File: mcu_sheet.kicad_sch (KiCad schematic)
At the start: 27 parts, among them IC1 STM32H523CET6, J1 Conn_01x05, SW1 SW_Push, SW2 SW_SPDT, Y1 Crystal_GND23, Y2 Crystal

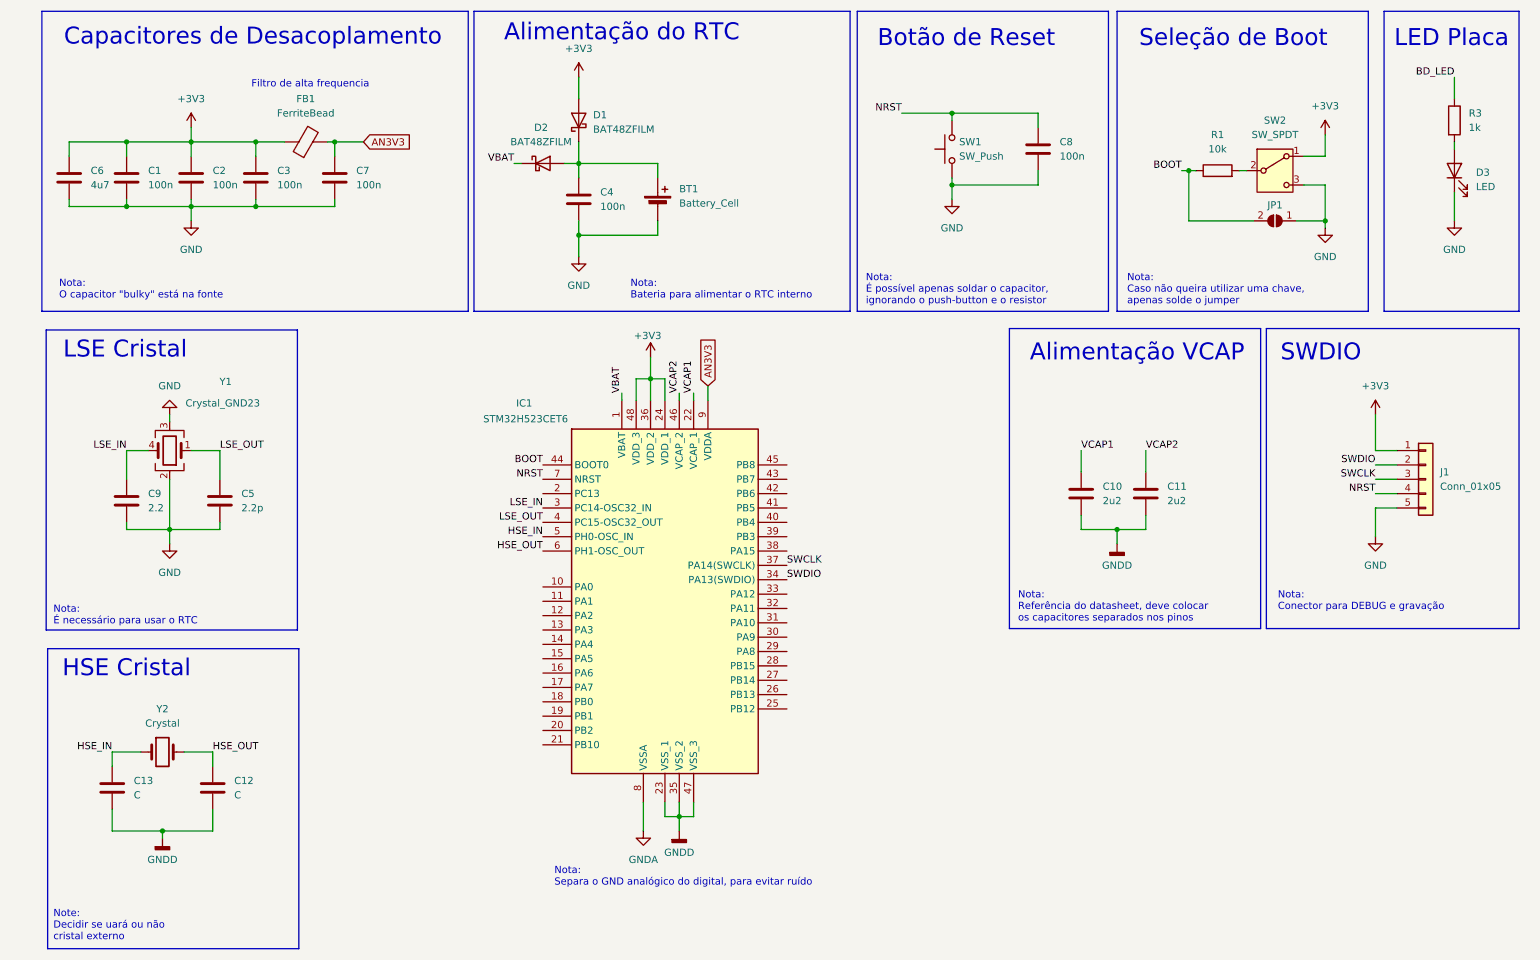
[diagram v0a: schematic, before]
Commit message: Alterei o nome para o par diferencial do CAN, adicionei capacitores de desacoplamento para todas as alimentacoes
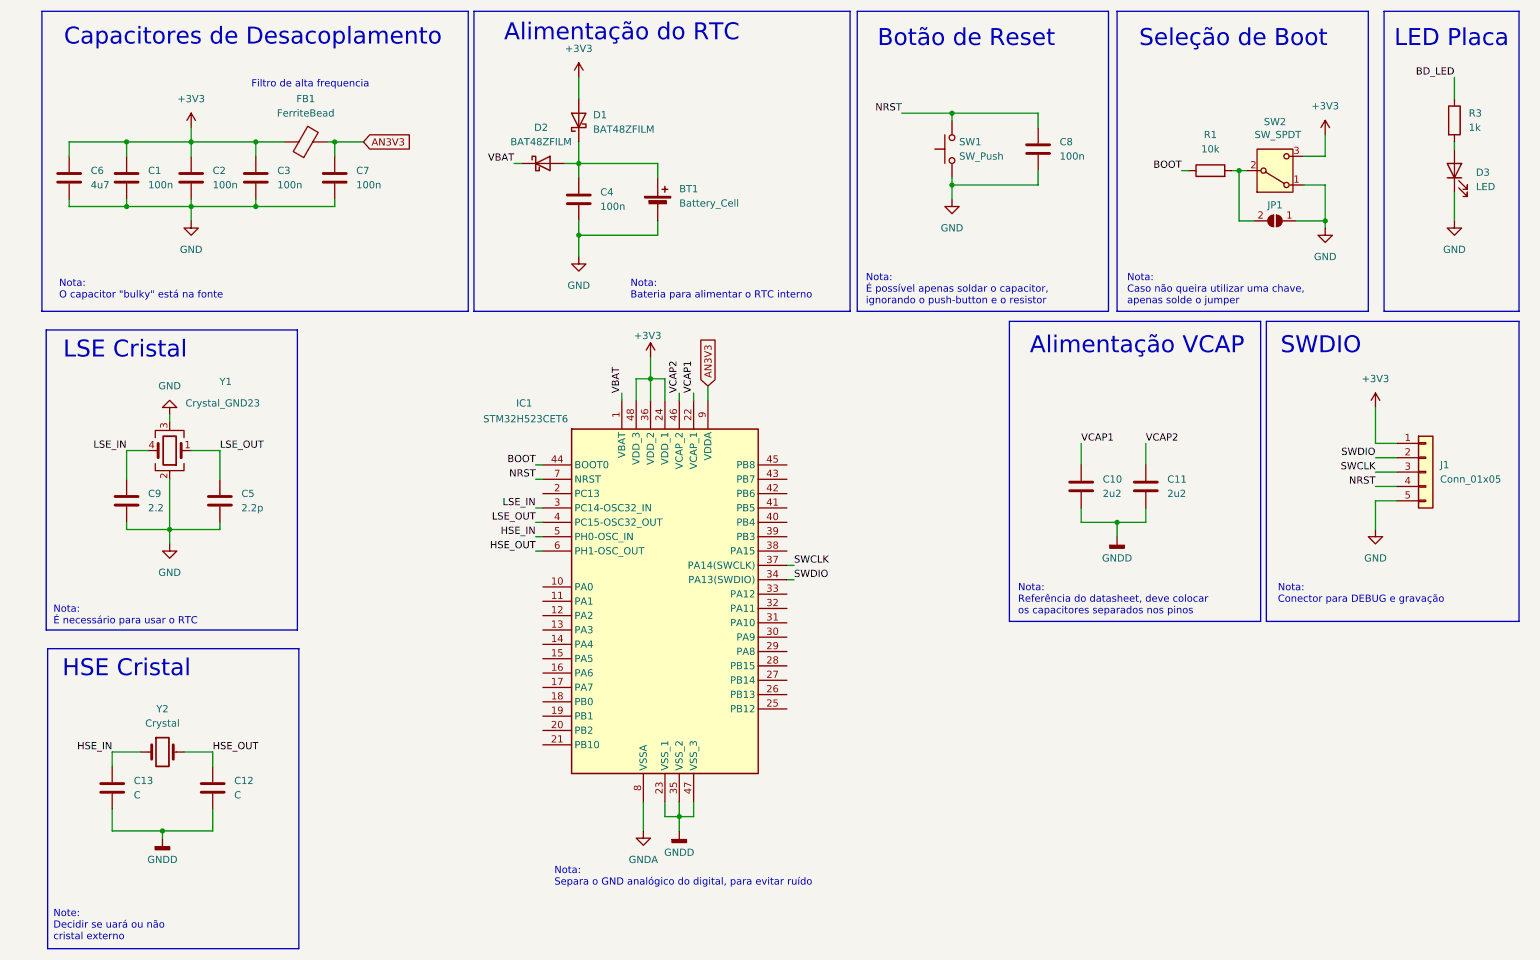
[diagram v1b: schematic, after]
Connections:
- net +3V3: now also SW2.3 (C); no longer SW2.1 (A)
- net BOOT: no longer JP1.2 (B)
- net GND: now also SW2.1 (A); no longer SW2.3 (C)
- net at R1.2, SW2.2 (B): now also JP1.2 (B)
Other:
- moved on the sheet: C10, C11, J1, R1

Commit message: Removi as entradas analógicas, projeto delas estava errado
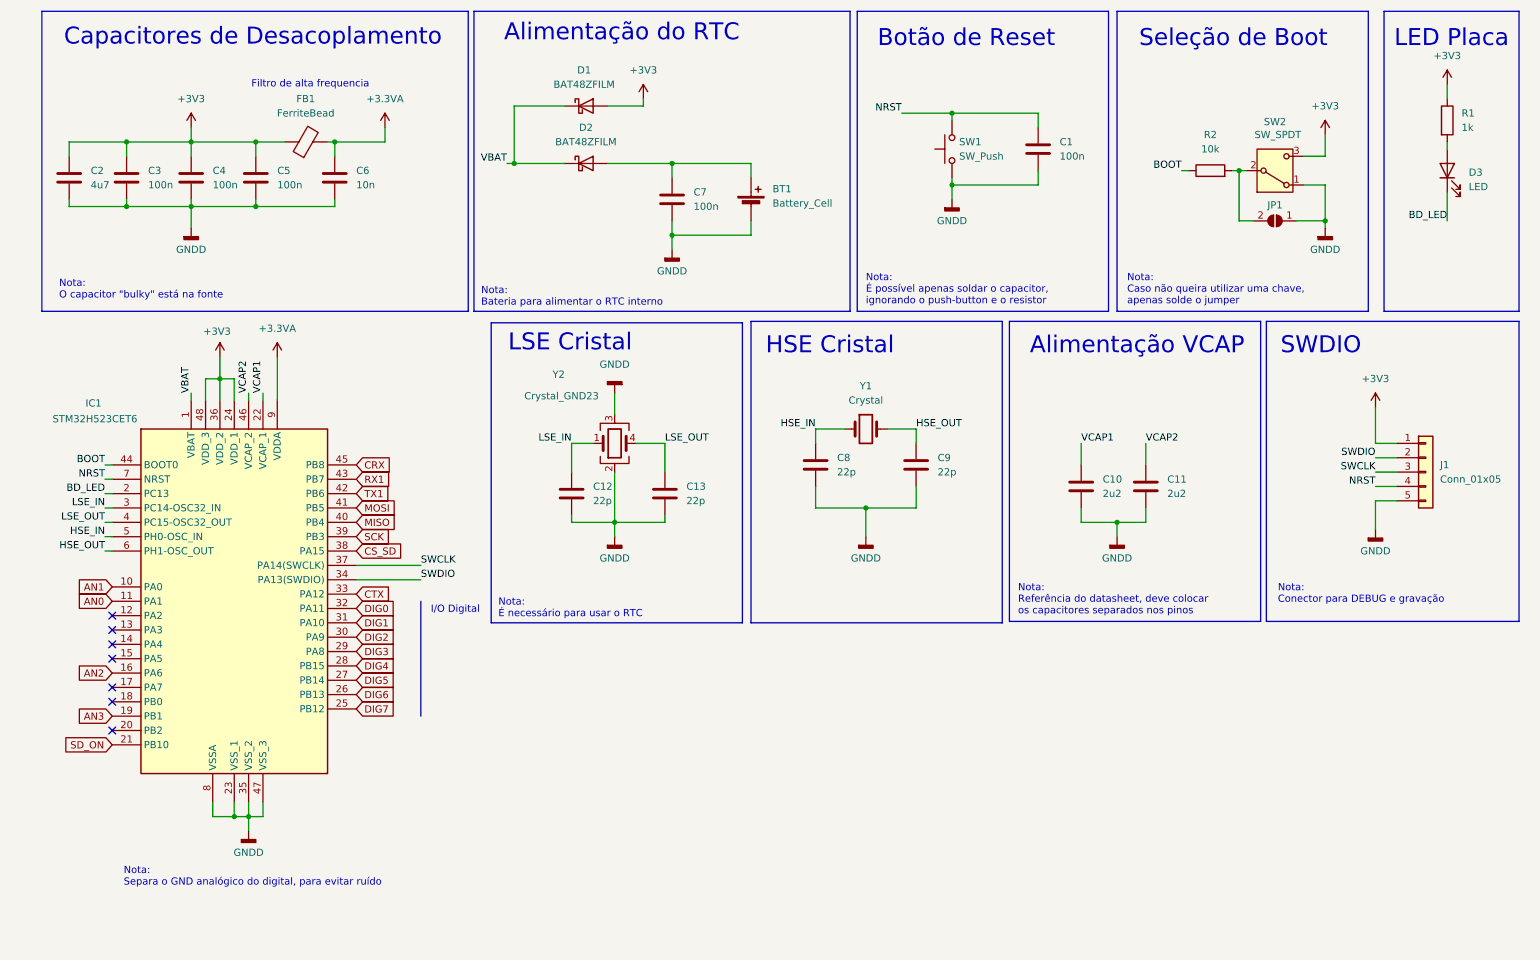
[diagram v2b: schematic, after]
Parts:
- BT1: footprint (none) -> Battery:BatteryHolder_MYOUNG_BS-07-A1BJ001_CR2032
- C1: renamed from C8; footprint (none) -> Capacitor_SMD:C_0603_1608Metric_Pad1.08x0.95mm_HandSolder
- C10, C11: footprint (none) -> Capacitor_SMD:C_0603_1608Metric_Pad1.08x0.95mm_HandSolder
- C12: renamed from C9; value 2.2 -> 22p; footprint (none) -> Capacitor_SMD:C_0603_1608Metric_Pad1.08x0.95mm_HandSolder
- C13: renamed from C5; value 2.2p -> 22p; footprint (none) -> Capacitor_SMD:C_0603_1608Metric_Pad1.08x0.95mm_HandSolder
- C2: renamed from C6; footprint (none) -> Capacitor_SMD:C_0805_2012Metric_Pad1.18x1.45mm_HandSolder
- C3: renamed from C1; footprint (none) -> Capacitor_SMD:C_0603_1608Metric_Pad1.08x0.95mm_HandSolder
- C4: renamed from C2; footprint (none) -> Capacitor_SMD:C_0603_1608Metric_Pad1.08x0.95mm_HandSolder
- C5: renamed from C3; footprint (none) -> Capacitor_SMD:C_0603_1608Metric_Pad1.08x0.95mm_HandSolder
- C6: renamed from C7; value 100n -> 10n; footprint (none) -> Capacitor_SMD:C_0603_1608Metric_Pad1.08x0.95mm_HandSolder
- C7: renamed from C4; footprint (none) -> Capacitor_SMD:C_0603_1608Metric_Pad1.08x0.95mm_HandSolder
- C8: renamed from C13; value C -> 22p; footprint (none) -> Capacitor_SMD:C_0603_1608Metric_Pad1.08x0.95mm_HandSolder
- C9: renamed from C12; value C -> 22p; footprint (none) -> Capacitor_SMD:C_0603_1608Metric_Pad1.08x0.95mm_HandSolder
- D3: footprint BajaKICAD:LED_1210_HandSoldering -> Baja_Library:LED_1210_HandSoldering
- IC1: footprint QFP50P900X900X160-48N -> Baja_Library:QFP50P900X900X160-48N
- J1: footprint Connector_PinHeader_2.54mm:PinHeader_1x05_P2.54mm_Horizontal -> Connector_PinHeader_2.54mm:PinHeader_1x05_P2.54mm_Vertical
- R2: renamed from R1; footprint Resistor_SMD:R_1206_3216Metric -> Resistor_SMD:R_1206_3216Metric_Pad1.30x1.75mm_HandSolder
- SW2: footprint Button_Switch_THT:SW_Slide_SPDT_Straight_CK_OS102011MS2Q -> Connector_PinHeader_2.54mm:PinHeader_1x03_P2.54mm_Vertical
- Y1: renamed from Y2; footprint (none) -> Crystal:Crystal_SMD_HC49-SD_HandSoldering
- Y2: renamed from Y1; footprint (none) -> Baja_Library:DMX-26S
- renumbered R3 to R1
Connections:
- net GNDA is gone; now on net GNDD: IC1.8 (VSSA)
- net +3V3: now also R1.1
- net BD_LED: now also D3.1 (K), IC1.2 (PC13); no longer R1.1
- net GNDD: now also BT1.2 (-), C1.2, C12.2, C13.2, C2.2, C3.2, C4.2, C5.2, C6.2, C7.2, J1.5 (Pin_5), JP1.1 (A), SW1.1, SW2.1 (A), Y2.2, Y2.3
- net LSE_IN: now also Y2.1; no longer Y2.4
- net LSE_OUT: now also Y2.4; no longer Y2.1
- net VBAT: now also D1.1 (K)
- net AN1: now reaches IC1.10 (PA0)
- net AN0: now reaches IC1.11 (PA1)
- net AN2: now reaches IC1.16 (PA6)
- net AN3: now reaches IC1.19 (PB1)
- net SD_ON: now reaches IC1.21 (PB10)
- net DIG7: now reaches IC1.25 (PB12)
- net DIG6: now reaches IC1.26 (PB13)
- net DIG5: now reaches IC1.27 (PB14)
- net DIG4: now reaches IC1.28 (PB15)
- net DIG3: now reaches IC1.29 (PA8)
- net DIG2: now reaches IC1.30 (PA9)
- net DIG1: now reaches IC1.31 (PA10)
- net DIG0: now reaches IC1.32 (PA11)
- net CTX: now reaches IC1.33 (PA12)
- net CS_SD: now reaches IC1.38 (PA15)
- net SCK: now reaches IC1.39 (PB3)
- net MISO: now reaches IC1.40 (PB4)
- net MOSI: now reaches IC1.41 (PB5)
- net TX1: now reaches IC1.42 (PB6)
- net RX1: now reaches IC1.43 (PB7)
- net CRX: now reaches IC1.45 (PB8)
- net at BT1.1 (+), C7.1, D2.2 (A): no longer D1.1 (K)
- net AN3V3 renamed +3.3VA
- removed net GND: BT1.2 (-), C1.2, C12.2, C13.2, C2.2, C3.2, C4.2, C5.2, C6.2, C7.2, D3.1 (K), J1.5 (Pin_5), JP1.1 (A), SW1.1, SW2.1 (A), Y2.2, Y2.3
- no-connect marks 0 -> 7
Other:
- note added: "I/O Digital"
- note removed: "Note: Decidir se uará ou não cristal externo"
- moved on the sheet: BT1, C12, C13, C7, C8, C9, D1, D2, D3, IC1, R1, Y1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

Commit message: Alterei para ter 3 portas analogicas, adaptei o circuito do RPM para ter um jumper que permite usar como entrada digital
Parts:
- renumbered C2 to C1, C3 to C2, C4 to C3, C5 to C4, C6 to C5, C7 to C6, C1 to C7, SW2 to SW1, SW1 to SW2
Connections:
- net NTC_AN_3: now reaches IC1.12 (PA2)
- net AN0 renamed NTC_AN_2
- net AN1 renamed NTC_AN_1
- net AN2: no longer names the net of IC1.16 (PA6)
- net AN3: no longer names the net of IC1.19 (PB1)
- net DIG4: no longer names the net of IC1.28 (PB15)
- net DIG5: no longer names the net of IC1.27 (PB14)
- net DIG6: no longer names the net of IC1.26 (PB13)
- net DIG7: no longer names the net of IC1.25 (PB12)
- net GNDD renamed GND
- no-connect marks 7 -> 12
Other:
- moved on the sheet: BT1, C6, C7, D1, D2, SW2

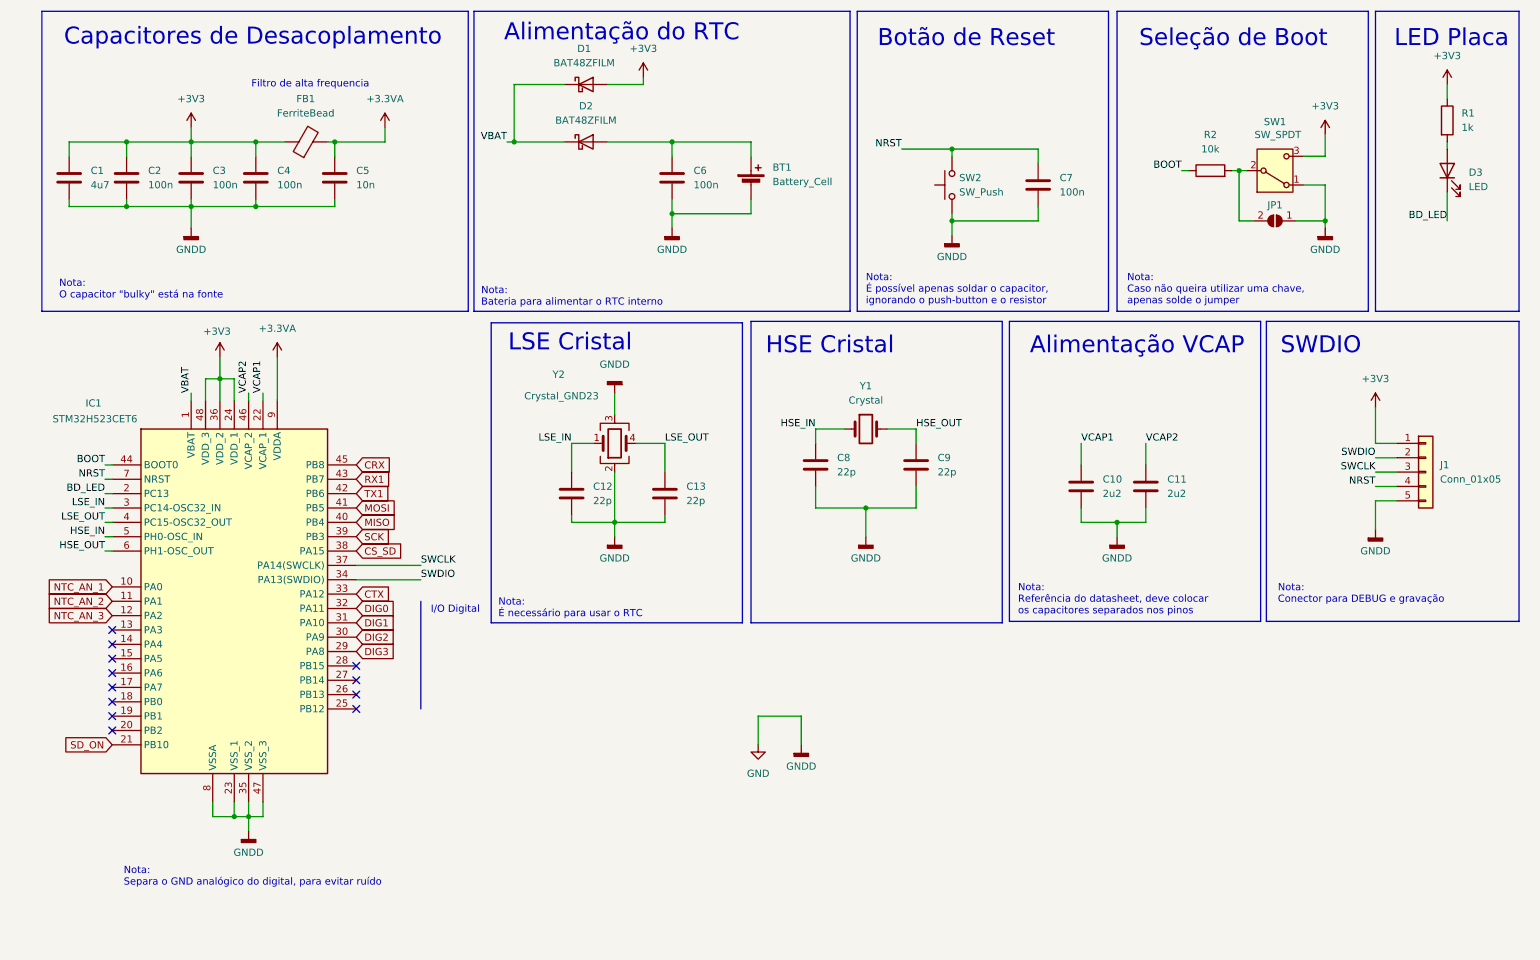
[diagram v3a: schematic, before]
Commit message: Diminui o tamanho da placa
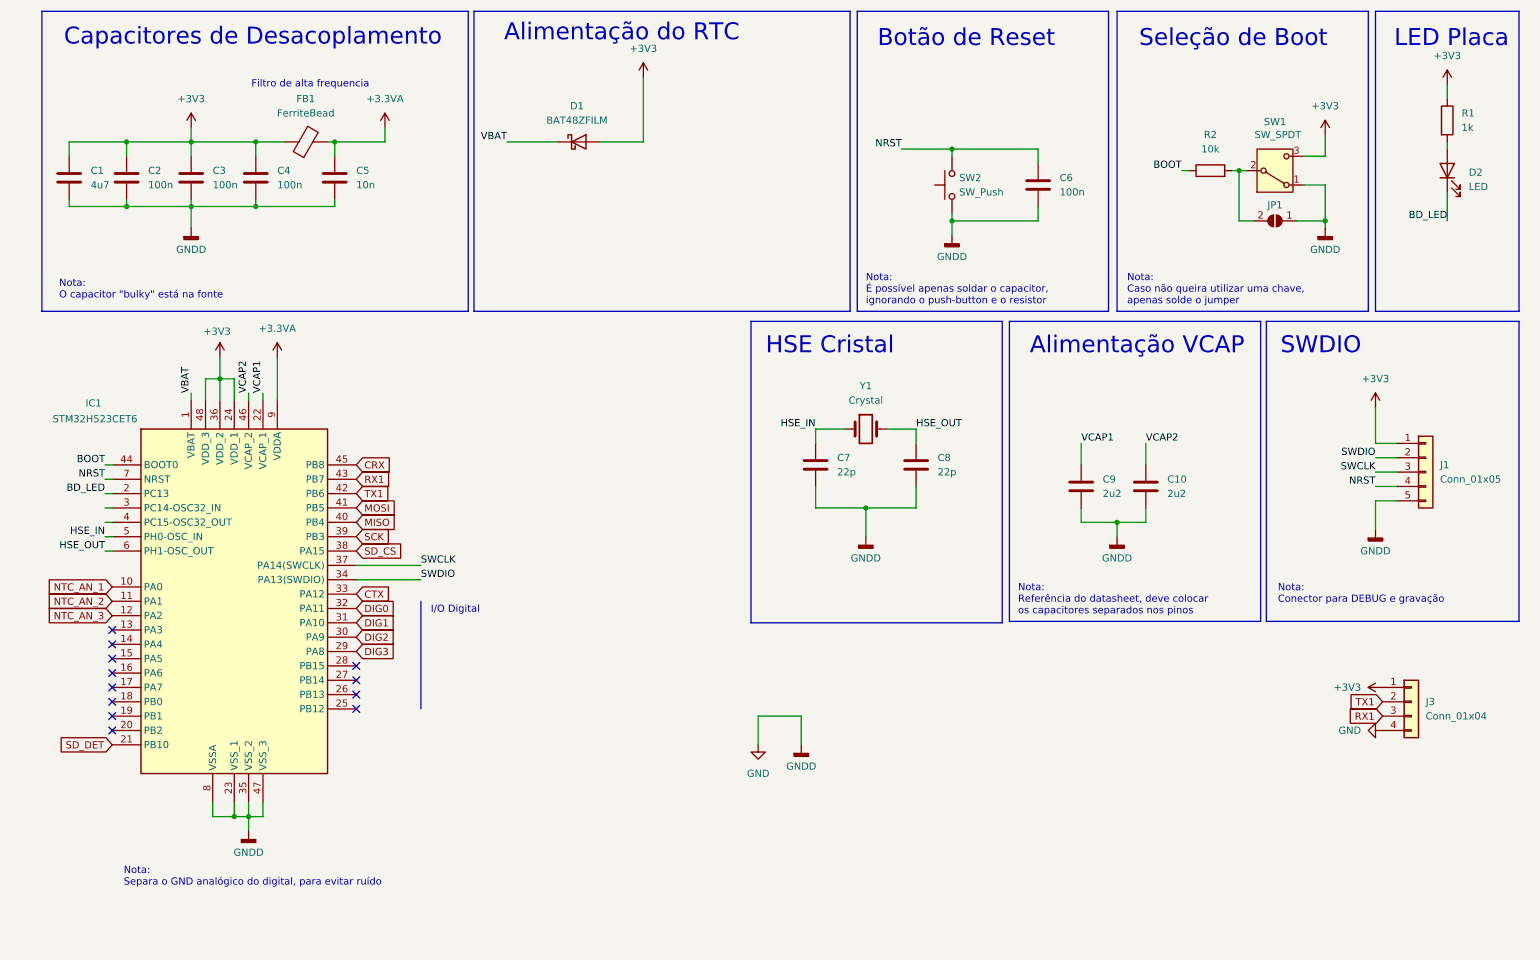
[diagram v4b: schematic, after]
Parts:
- removed BT1: Battery_Cell, Battery:BatteryHolder_MYOUNG_BS-07-A1BJ001_CR2032, symbol Device:Battery_Cell
- removed C12, C13: 22p, Capacitor_SMD:C_0603_1608Metric_Pad1.08x0.95mm_HandSolder, symbol Device:C
- removed C6: 100n, Capacitor_SMD:C_0603_1608Metric_Pad1.08x0.95mm_HandSolder, symbol Device:C
- removed D2: BAT48ZFILM, Diode_SMD:D_SOD-123, symbol Diode:BAT48ZFILM
- removed Y2: Crystal_GND23, Baja_Library:DMX-26S, symbol Device:Crystal_GND23
- added J3: Conn_01x04, Baja_Library:Molex_KK-254_AE-6410-04A_1x04_P2.54mm_Vertical, symbol Connector_Generic:Conn_01x04
- JP1: footprint Jumper:SolderJumper-2_P1.3mm_Open_Pad1.0x1.5mm -> Jumper:SolderJumper-2_P1.3mm_Open_RoundedPad1.0x1.5mm
- renumbered C11 to C10, C7 to C6, C8 to C7, C9 to C8, C10 to C9, D3 to D2
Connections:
- net +3V3: now also J3.1 (Pin_1)
- net GND: now also J3.4 (Pin_4)
- net RX1: now also J3.3 (Pin_3)
- net TX1: now also J3.2 (Pin_2)
- net CS_SD renamed SD_CS
- net LSE_IN: no longer names the net of IC1.3 (PC14-OSC32_IN)
- net LSE_OUT: no longer names the net of IC1.4 (PC15-OSC32_OUT)
- net SD_ON renamed SD_DET
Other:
- note removed: "LSE Cristal"
- note removed: "Nota: Bateria para alimentar o RTC interno"
- note removed: "Nota: É necessário para usar o RTC"
- moved on the sheet: D1
